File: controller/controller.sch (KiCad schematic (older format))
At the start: 31 parts, among them J1 ICSP, J2 USB_B_Micro, J3 TRRS_Jack, J6 6P_ZH_connector, J7 6P_ZH_connector, SW1 RESET, U3 ATmega32U4-AU, Y1 16MHz

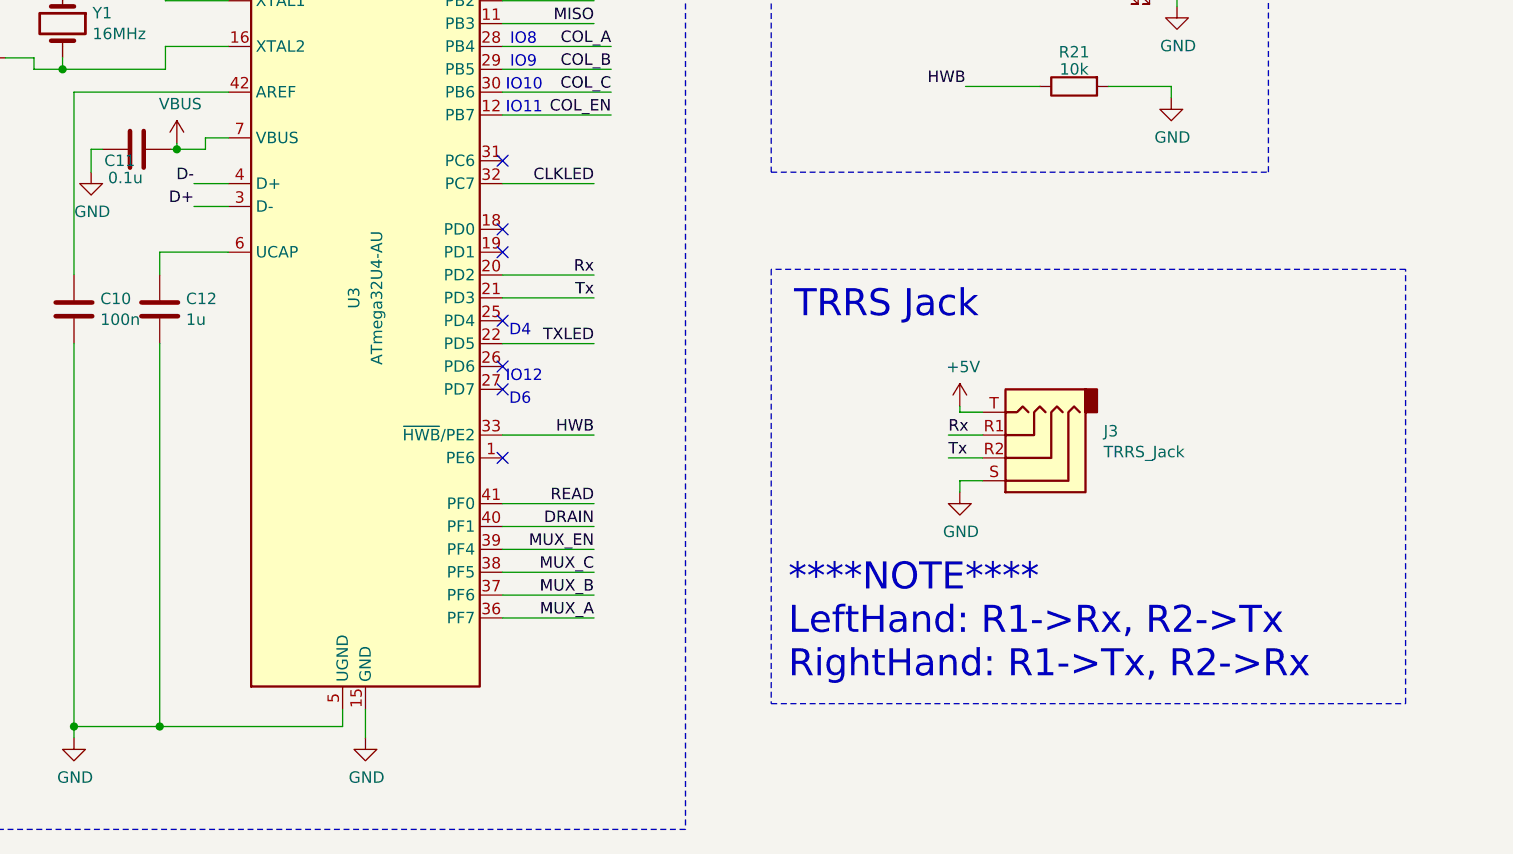
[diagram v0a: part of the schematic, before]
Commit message: [fix] D-/D+ flip [add] smd jumper for Tx/Rx selection
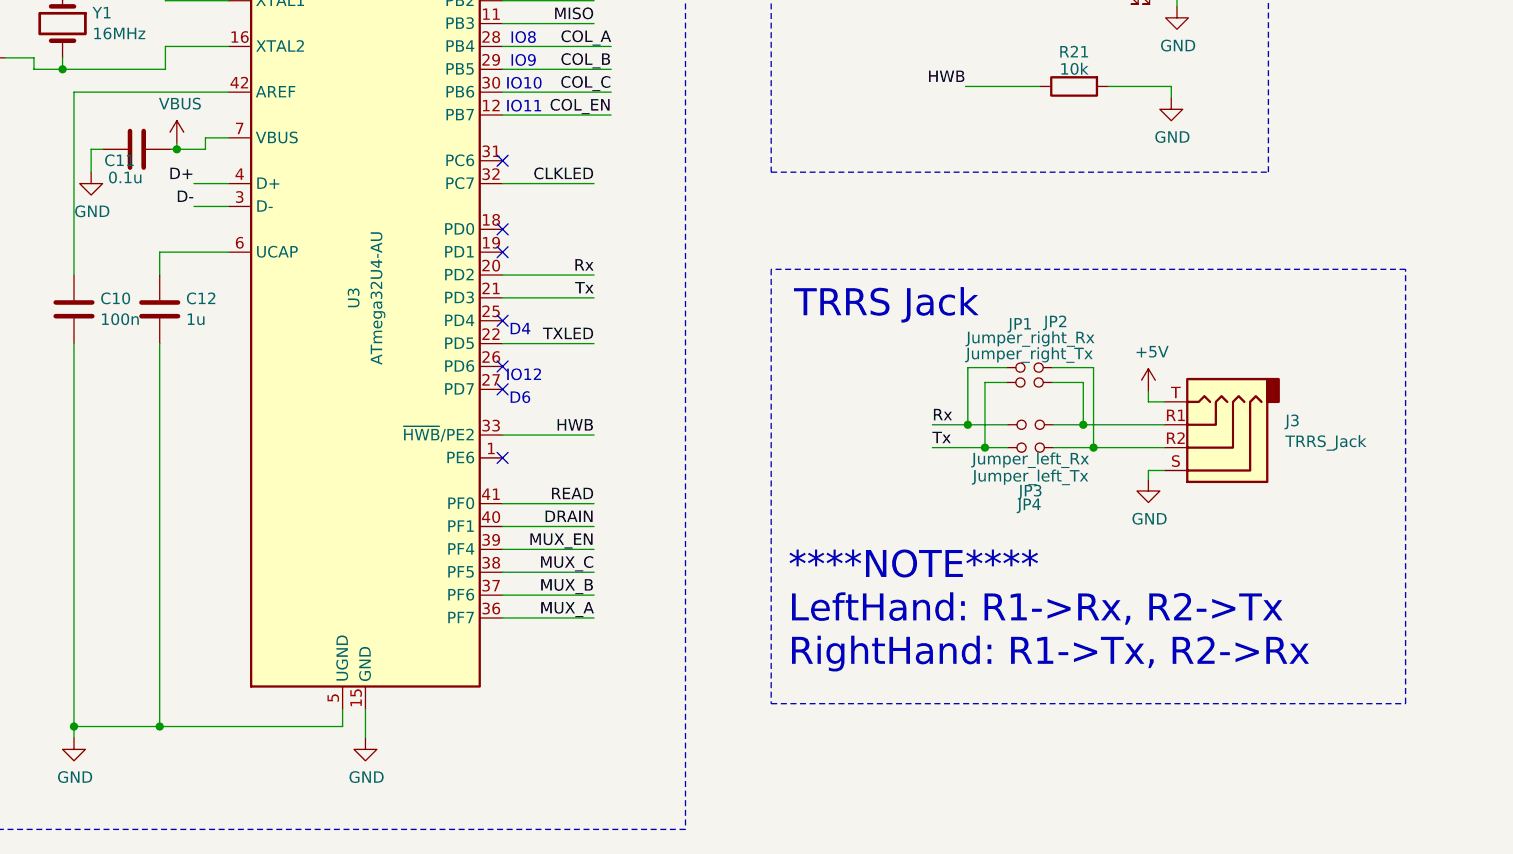
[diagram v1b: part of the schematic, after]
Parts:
- added JP1: Jumper_right_Tx, MyLib:soldering_jumper_W0.8_P0.2, symbol Device:Jumper_NO_Small
- added JP2: Jumper_right_Rx, MyLib:soldering_jumper_W0.8_P0.2, symbol Device:Jumper_NO_Small
- added JP3: Jumper_left_Rx, MyLib:soldering_jumper_W0.8_P0.2, symbol Device:Jumper_NO_Small
- added JP4: Jumper_left_Tx, MyLib:soldering_jumper_W0.8_P0.2, symbol Device:Jumper_NO_Small
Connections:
- net D+: now also U3.4 (D+); no longer U3.3 (D-)
- net D-: now also U3.3 (D-); no longer U3.4 (D+)
- net Rx: now also JP1.1, JP3.1; no longer J3.R1
- net Tx: now also JP2.1, JP4.1; no longer J3.R2
- new net: J3.R1, JP2.2, JP3.2
- new net: J3.R2, JP1.2, JP4.2
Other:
- moved on the sheet: J3
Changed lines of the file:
@@
 Wire Wire Line
 	4550 5900 4550 5950
+Text Label 5075 3625 2    50   ~ 0
+D-
 Text Label 5075 3525 2    50   ~ 0
-D-
-Text Label 5075 3625 2    50   ~ 0
 D+
 Wire Wire Line
@@
 Wire Wire Line
 	6825 3925 6425 3925
-Text Label 8375 4725 0    50   ~ 0
-Tx
-Wire Wire Line
-	8375 4725 8525 4725
-Text Label 8375 4625 0    50   ~ 0
+Text Label 8305 4580 0    50   ~ 0
 Rx
-Wire Wire Line
-	8375 4625 8525 4625
-Text Notes 7675 5700 0    118  ~ 0
+Text Notes 7675 5650 0    118  ~ 0
 ****NOTE****\nLeftHand: R1->Rx, R2->Tx\nRightHand: R1->Tx, R2->Rx
-$Comp
-L power:+5V #PWR033
-U 1 1 5EFD17DC
-P 8425 4500
-F 0 "#PWR033" H 8425 4350 50  0001 C CNN
-F 1 "+5V" H 8440 4673 50  0000 C CNN
-F 2 "" H 8425 4500 50  0001 C CNN
-F 3 "" H 8425 4500 50  0001 C CNN
-	1    8425 4500
-	1    0    0    -1
-$EndComp
-Wire Wire Line
-	8425 4500 8425 4525
-Wire Wire Line
-	8425 4525 8525 4525
-$Comp
-L power:GND #PWR034
-U 1 1 5EFD9894
-P 8425 4875
-F 0 "#PWR034" H 8425 4625 50  0001 C CNN
-F 1 "GND" H 8430 4702 50  0000 C CNN
-F 2 "" H 8425 4875 50  0001 C CNN
-F 3 "" H 8425 4875 50  0001 C CNN
-	1    8425 4875
-	1    0    0    -1
-$EndComp
-Wire Wire Line
-	8425 4875 8425 4825
 $Comp
 L Connector:AudioJack4 J3
 U 1 1 5EFE9CF0
-P 8725 4725
-F 0 "J3" H 8396 4608 50  0000 R CNN
-F 1 "TRRS_Jack" H 8396 4699 50  0000 R CNN
-F 2 "MyLib:TRRS_jack_MJ4PP9" H 8725 4725 50  0001 C CNN
-F 3 "~" H 8725 4725 50  0001 C CNN
-	1    8725 4725
+P 9520 4680
+F 0 "J3" H 9191 4563 50  0000 R CNN
+F 1 "TRRS_Jack" H 9191 4654 50  0000 R CNN
+F 2 "MyLib:TRRS_jack_MJ4PP9" H 9520 4680 50  0001 C CNN
+F 3 "~" H 9520 4680 50  0001 C CNN
+	1    9520 4680
 	-1   0    0    1
 $EndComp
-Wire Wire Line
-	8425 4825 8525 4825
 Wire Notes Line
 	7225 1225 7225 6350
@@
 Split HHKB Controller Board
 NoConn ~ 6425 4125
+$Comp
+L Device:Jumper_NO_Small JP3
+U 1 1 5EEEE665
+P 8735 4580
+F 0 "JP3" H 8735 4290 50  0000 C CNN
+F 1 "Jumper_left_Rx" H 8735 4430 50  0000 C CNN
+F 2 "MyLib:soldering_jumper_W0.8_P0.2" H 8735 4580 50  0001 C CNN
+F 3 "~" H 8735 4580 50  0001 C CNN
+	1    8735 4580
+	1    0    0    -1
+$EndComp
+$Comp
+L Device:Jumper_NO_Small JP4
+U 1 1 5EF06B1A
+P 8735 4680
+F 0 "JP4" H 8730 4430 50  0000 C CNN
+F 1 "Jumper_left_Tx" H 8735 4555 50  0000 C CNN
+F 2 "MyLib:soldering_jumper_W0.8_P0.2" H 8735 4680 50  0001 C CNN
+F 3 "~" H 8735 4680 50  0001 C CNN
+	1    8735 4680
+	1    0    0    -1
+$EndComp
+Wire Wire Line
+	8835 4680 9010 4680
+Wire Wire Line
+	8835 4580 8965 4580
+Wire Wire Line
+	8635 4580 8460 4580
+Text Label 8305 4680 0    50   ~ 0
+Tx
+Wire Wire Line
+	8635 4680 8535 4680
+$Comp
+L Device:Jumper_NO_Small JP2
+U 1 1 5F036E22
+P 8730 4395
+F 0 "JP2" H 8845 4660 50  0000 C CNN
+F 1 "Jumper_right_Rx" H 8735 4590 50  0000 C CNN
+F 2 "MyLib:soldering_jumper_W0.8_P0.2" H 8730 4395 50  0001 C CNN
+F 3 "~" H 8730 4395 50  0001 C CNN
+	1    8730 4395
+	1    0    0    -1
+$EndComp
+$Comp
+L Device:Jumper_NO_Small JP1
+U 1 1 5F036ED4
+P 8730 4330
+F 0 "JP1" H 8690 4520 50  0000 C CNN
+F 1 "Jumper_right_Tx" H 8730 4390 50  0000 C CNN
+F 2 "MyLib:soldering_jumper_W0.8_P0.2" H 8730 4330 50  0001 C CNN
+F 3 "~" H 8730 4330 50  0001 C CNN
+	1    8730 4330
+	1    0    0    -1
+$EndComp
+Wire Wire Line
+	8460 4580 8460 4330
+Wire Wire Line
+	8460 4330 8630 4330
+Connection ~ 8460 4580
+Wire Wire Line
+	8460 4580 8305 4580
+Wire Wire Line
+	8535 4680 8535 4395
+Wire Wire Line
+	8535 4395 8630 4395
+Connection ~ 8535 4680
+Wire Wire Line
+	8535 4680 8305 4680
+Wire Wire Line
+	8830 4395 8965 4395
+Wire Wire Line
+	8965 4395 8965 4580
+Connection ~ 8965 4580
+Wire Wire Line
+	8965 4580 9320 4580
+Wire Wire Line
+	8830 4330 9010 4330
+Wire Wire Line
+	9010 4330 9010 4680
+Connection ~ 9010 4680
+Wire Wire Line
+	9010 4680 9320 4680
+$Comp
+L power:GND #PWR0102
+U 1 1 5F059B65
+P 9250 4820
+F 0 "#PWR0102" H 9250 4570 50  0001 C CNN
+F 1 "GND" H 9255 4647 50  0000 C CNN
+F 2 "" H 9250 4820 50  0001 C CNN
+F 3 "" H 9250 4820 50  0001 C CNN
+	1    9250 4820
+	1    0    0    -1
+$EndComp
+Wire Wire Line
+	9250 4820 9250 4780
+Wire Wire Line
+	9250 4780 9320 4780
+$Comp
+L power:+5V #PWR0103
+U 1 1 5F062E45
+P 9250 4435
+F 0 "#PWR0103" H 9250 4285 50  0001 C CNN
+F 1 "+5V" H 9265 4608 50  0000 C CNN
+F 2 "" H 9250 4435 50  0001 C CNN
+F 3 "" H 9250 4435 50  0001 C CNN
+	1    9250 4435
+	1    0    0    -1
+$EndComp
+Wire Wire Line
+	9250 4435 9250 4480
+Wire Wire Line
+	9250 4480 9320 4480
 $EndSCHEMATC

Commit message: [add] lefthand gerber
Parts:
- J2: symbol Connector:USB_B_Micro -> controller-rescue:USB_B_Micro-Connector
- U3: symbol MCU_Microchip_ATmega:ATmega32U4-AU -> controller-rescue:ATmega32U4-AU-MCU_Microchip_ATmega
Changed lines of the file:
@@
 EESchema Schematic File Version 4
-LIBS:controller-cache
-EELAYER 26 0
+EELAYER 30 0
 EELAYER END
 $Descr A4 11693 8268
@@
 $EndDescr
 $Comp
-L MCU_Microchip_ATmega:ATmega32U4-AU U3
+L controller-rescue:ATmega32U4-AU-MCU_Microchip_ATmega U3
 U 1 1 5ECFFB58
 P 5825 4025
@@
 Connection ~ 6450 2150
 $Comp
-L Connector:USB_B_Micro J2
+L controller-rescue:USB_B_Micro-Connector J2
 U 1 1 5EDE139B
 P 1925 4750
